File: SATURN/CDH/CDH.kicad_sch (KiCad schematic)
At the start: 0 parts

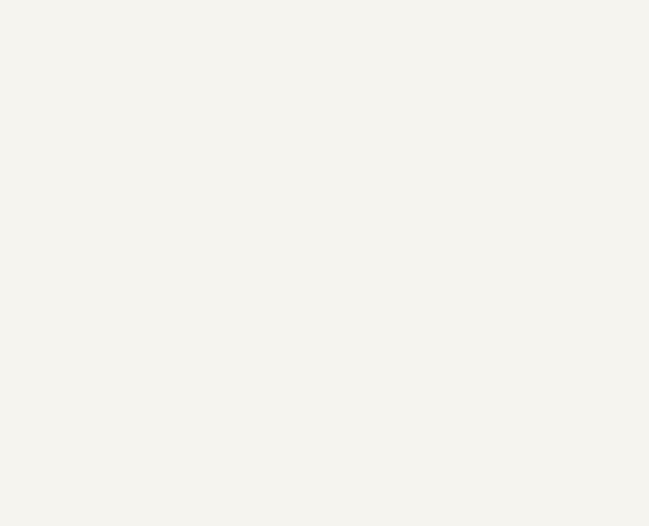
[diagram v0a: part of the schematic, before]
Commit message: Added memory, connections to MCUs
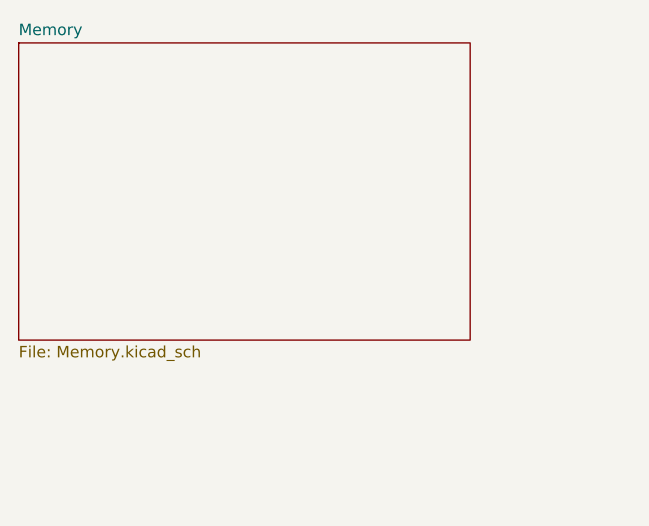
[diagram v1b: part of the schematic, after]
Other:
- added sheet Memory (Memory.kicad_sch)
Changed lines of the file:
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@@
 	(paper "A4")
+	(sheet
+		(at 35.56 72.39)
+		(size 50.165 33.02)
+		(exclude_from_sim no)
+		(in_bom yes)
+		(on_board yes)
+		(dnp no)
+		(fields_autoplaced yes)
+		(stroke
+			(width 0.1524)
+			(type solid)
+		)
+		(fill
+			(color 0 0 0 0)
+		)
+		(property "Sheetname" "Memory"
+			(at 35.56 71.6784 0)
+			(show_name no)
+			(do_not_autoplace no)
+			(effects
+				(font
+					(size 1.27 1.27)
+				)
+				(justify left bottom)
+			)
+		)
+		(property "Sheetfile" "Memory.kicad_sch"
+			(at 35.56 105.9946 0)
+			(show_name no)
+			(do_not_autoplace no)
+			(effects
+				(font
+					(size 1.27 1.27)
+				)
+				(justify left top)
+			)
+		)
+		(instances
+			(project "CDH"
+				(path "/100d4475-6c5b-4ca4-82f4-ff20798e9edf"
+					(page "3")
+				)
+			)
+		)
+	)
 	(sheet
 		(at 135.255 165.1)
@@
 		)
 		(instances
-			(project "OBC"
+			(project "CDH"
 				(path "/100d4475-6c5b-4ca4-82f4-ff20798e9edf"
 					(page "2")
